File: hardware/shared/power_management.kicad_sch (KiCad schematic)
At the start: 0 parts

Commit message: more kicad work
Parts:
- added C1, C11, C2: 1uF, Capacitor_SMD:C_0402_1005Metric, symbol Device:C
- added C10, C12, C13, C14, C4, C5, C7, C8, C9: 10uF, Capacitor_SMD:C_0603_1608Metric, symbol Device:C
- added C3: 4.7uF, Capacitor_SMD:C_0603_1608Metric, symbol Device:C
- added C6: 100nF, Capacitor_SMD:C_0402_1005Metric, symbol Device:C
- added D1: RED err, LED_SMD:LED_0603_1608Metric, symbol Device:LED
- added D2: GREEN chg, LED_SMD:LED_0603_1608Metric, symbol Device:LED
- added J3: USB4720-03-A, obc:GCT_USB4720-03-A_REVA, symbol obc:USB4720-03-A
- added J4: BT1 1S Li-Po, Connector_JST:JST_PH_S2B-PH-K_1x02_P2.00mm_Horizontal, symbol Connector_Generic:Conn_01x02
- added L1, L2, L3: 2.2uH, Inductor_SMD:L_Murata_DFE201610P, symbol Device:L
- added R6: 10k 1%, Resistor_SMD:R_0402_1005Metric, symbol Device:R
- added R7: 300k 1%, Resistor_SMD:R_0402_1005Metric, symbol Device:R
- added SW5: PWR, Button_Switch_SMD:SW_SPST_EVQP7C, symbol Switch:SW_Push
- added U2: NPM1300-CAAA-R, obc:BGA35N44X41P5X7_237X307X51, symbol obc:NPM1300-CAAA-R
- added U7: TPS610997, symbol obc:TPS610997
- added U8: USBLC6-2SC6, Package_TO_SOT_SMD:SOT-23-6, symbol Power_Protection:USBLC6-2SC6
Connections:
- new net: SW5.2, U2.D4 (SHPHLD)
- new net: L3.2, U7.5 (SW)
- new net: L1.1, U2.B7 (SW1)
- new net: D1.1 (K), U2.A1 (LED0)
- new net: D2.1 (K), U2.A2 (LED1)
- new net: R6.1, U2.D3 (NTC)
- new net: L2.1, U2.D7 (SW2)
- new net: R7.1, U2.E1 (VSET2)
- new net +1V8_MAG: C10.1, C9.1, U2.A4 (LSOUT1/VOUTLDO1)
- new net +3V3: C6.1, C8.1, L2.2, U2.B4 (LSIN1/VINLDO1), U2.B5 (LSIN2/VINLDO2), U2.C6 (VOUT2), U2.E4 (VDDIO)
- new net +3V3_GPS: C11.1, U2.A5 (LSOUT2/VOUTLDO2)
- new net +3V3_SD: C7.1, L1.2, U2.B6 (VOUT1)
- new net +5V_DISP: C13.1, C14.1, U7.2 (VOUT)
- new net DISP_5V_EN: U7.4 (EN)
- new net GND: C1.2, C10.2, C11.2, C12.2, C13.2, C14.2, C2.2, C3.2, C4.2, C5.2, C6.2, C7.2, C8.2, C9.2, J3.A1_B12 (GND_A), J3.B1_A12 (GND_B), J3.SH1 (SHIELD), J3.SH2 (SHIELD), J3.SH3 (SHIELD), J3.SH4 (SHIELD), J3.SH5 (SHIELD), J3.SH6 (SHIELD), J4.2 (Pin_2), R6.2, R7.2, SW5.1, U2.A6 (AVSS), U2.A7 (PVSS1), U2.E2 (VSET1), U2.E7 (PVSS2), U7.1 (GND), U7.3 (FB), U7.7 (PAD), U8.2 (GND)
- new net PMIC_INT: U2.C4 (GPIO3)
- new net SCL: U2.E3 (SCL)
- new net SDA: U2.E5 (SDA)
- new net USB_CC1: J3.A5 (CC1), U2.D5 (CC1)
- new net USB_CC2: J3.B5 (CC2), U2.B3 (CC2)
- new net USB_DM: J3.A7 (DN1), J3.B7 (DN2), U8.1 (I/O1), U8.6 (I/O1)
- new net USB_DP: J3.A6 (DP1), J3.B6 (DP2), U8.3 (I/O2), U8.4 (I/O2)
- new net VBAT: C3.1, J4.1 (Pin_1), U2.D1 (VBAT), U2.D2 (VBAT)
- new net VBUS: C1.1, J3.A4_B9 (VBUS_A), J3.B4_A9 (VBUS_B), U2.B1 (VBUS), U2.B2 (VBUS), U8.5 (VBUS)
- new net VBUS_MCU: C2.1, U2.C3 (VBUSOUT)
- new net VSYS: C12.1, C4.1, C5.1, D1.2 (A), D2.2 (A), L3.1, U2.C1 (VSYS), U2.C2 (VSYS), U2.C7 (PVDD), U7.6 (VIN)
- no-connect marks 0 -> 6
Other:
- note added: "5V DISPLAY BOOST — TPS610997"
- note added: "BATTERY"
- note added: "ERC FLAGS"
- note added: "PVDD"
- note added: "USB-C"
- note added: "VBUSOUT"
- note added: "VSET2=300k -> BUCK2 3.3V at startup (main rail). VSET1=GND -> BUCK1 OFF at startup; fw sets 3.3V, enables only to mount SD (power gate). LDSW1 = LDO 1.8V from +3V3 -> BMM350 VDD. LDSW2 = load switch +3V3 -> +3V3_GPS. Both OFF at boot - fw enables via I2C (0x6B). Charge current set in fw; NTC fixed 10k (no pack thermistor) -> disable NTC monitor or treat 25C. LED0 = charger error, LED1 = charging 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"
- note added: "nPM1300 — CHARGER + BUCKS + LDSW"
- note added: "pack NTC: n/a (R6 fixed)"
- company: (none) -> OpenBikeComputer
- title: (none) -> Power Management

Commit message: more pcb work - add baseboard remove Proto
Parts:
- removed C1, C11, C2: 1uF, Capacitor_SMD:C_0402_1005Metric, symbol Device:C
- removed C10, C4, C5, C7, C8, C9: 10uF, Capacitor_SMD:C_0603_1608Metric, symbol Device:C
- removed C3: 4.7uF, Capacitor_SMD:C_0603_1608Metric, symbol Device:C
- removed C6: 100nF, Capacitor_SMD:C_0402_1005Metric, symbol Device:C
- removed D1: RED err, LED_SMD:LED_0603_1608Metric, symbol Device:LED
- removed D2: GREEN chg, LED_SMD:LED_0603_1608Metric, symbol Device:LED
- removed J3: USB4720-03-A, obc:GCT_USB4720-03-A_REVA, symbol obc:USB4720-03-A
- removed L1, L2: 2.2uH, Inductor_SMD:L_Murata_DFE201610P, symbol Device:L
- removed R6: 10k 1%, Resistor_SMD:R_0402_1005Metric, symbol Device:R
- removed R7: 300k 1%, Resistor_SMD:R_0402_1005Metric, symbol Device:R
- removed SW5: PWR, Button_Switch_SMD:SW_SPST_EVQP7C, symbol Switch:SW_Push
- removed U8: USBLC6-2SC6, Package_TO_SOT_SMD:SOT-23-6, symbol Power_Protection:USBLC6-2SC6
- added J3: Conn_01x06, symbol Connector_Generic:Conn_01x06
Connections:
- net GND: now also U2.D3 (NTC), J3.2 (Pin_2); no longer U2.A6 (AVSS), U2.A7 (PVSS1), U2.E2 (VSET1), U2.E7 (PVSS2)
- net SCL: now also U2.E5 (SDA); no longer U2.E3 (SCL)
- net SDA: now also U2.E3 (SCL); no longer U2.E5 (SDA)
- net USB_CC1: now also J3.3 (Pin_3)
- net USB_CC2: now also J3.4 (Pin_4)
- net USB_DM: now also J3.6 (Pin_6)
- net USB_DP: now also J3.5 (Pin_5)
- net VBUS: now also J3.1 (Pin_1)
- net VSYS: no longer U2.C1 (VSYS), U2.C2 (VSYS), U2.C7 (PVDD)
- net +1V8_MAG: no longer names the net of U2.A4 (LSOUT1/VOUTLDO1)
- removed net +3V3: U2.B4 (LSIN1/VINLDO1), U2.B5 (LSIN2/VINLDO2), U2.C6 (VOUT2), U2.E4 (VDDIO)
- net +3V3_GPS: no longer names the net of U2.A5 (LSOUT2/VOUTLDO2)
- net +3V3_SD: no longer names the net of U2.B6 (VOUT1)
- net PMIC_INT: no longer names the net of U2.C4 (GPIO3)
- net VBUS_MCU: no longer names the net of U2.C3 (VBUSOUT)
- no-connect marks 6 -> 3
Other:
- note added: "BUCK1 for SD Card"
- note added: "BUCK2 for everything else, 3.2V to make display very happy"
- note added: "LDO1 for 1.8V Compass"
- note added: "Loadswitch 2 for GPS"
- note removed: "PVDD"
- note removed: "VBUSOUT"
- note removed: "VSET2=300k -> BUCK2 3.3V at startup (main rail). VSET1=GND -> BUCK1 OFF at startup; fw sets 3.3V, enables only to mount SD (power gate). LDSW1 = LDO 1.8V from +3V3 -> BMM350 VDD. LDSW2 = load switch +3V3 -> +3V3_GPS. Both OFF at boot - fw enables via I2C (0x6B). Charge current set in fw; NTC fixed 10k (no pack thermistor) -> disable NTC monitor or treat 25C. LED0 = charger error, LED1 = charging 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"
- note removed: "pack NTC: n/a (R6 fixed)"
- moved on the sheet: C12, C13, C14, J4, L3, U7

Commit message: more schematic progress and some library additions
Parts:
- removed C12, C13, C14: 10uF, Capacitor_SMD:C_0603_1608Metric, symbol Device:C
- removed L3: 2.2uH, Inductor_SMD:L_Murata_DFE201610P, symbol Device:L
- added C1, C10, C2, C3, C4, C5, C8, C9: 10u, symbol Device:C_Small
- added C6: 1u, symbol Device:C_Small
- added C7: 100n, symbol Device:C_Small
- added L1, L2, L5: 2.2uH, symbol Device:L_Small
- added NT1, NT2: NetTie_2, symbol Device:NetTie_2
- added R1: 0R, symbol Device:R_Small
- added R2: 150k, symbol Device:R_Small
- U7: footprint (none) -> Package_SON:WSON-6-1EP_2x2mm_P0.65mm_EP1x1.6mm; MPN (none) -> TPS610997DRVR; Manufacturer (none) -> Texas Instruments
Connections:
- net +5V_DISP: now also U7.B2 (VOUT), C10.1, C9.1; no longer U7.2 (VOUT)
- net DISP_5V_EN: now also U7.C1 (EN); no longer U7.4 (EN)
- net GND: now also U2.A6 (AVSS), U7.A2 (GND), U7.C2 (FB), C10.2, C5.2, C6.2, C7.2, C8.2, C9.2, NT1.2, NT2.2, R1.2, R2.2; no longer U7.1 (GND), U7.3 (FB), U7.7 (PAD)
- net VBAT: now also U7.A1 (VIN), C8.1, L5.1
- net +1V8_MAG: now reaches U2.A4 (LSOUT1/VOUTLDO1)
- net +3V2_GPS: now reaches U2.A5 (LSOUT2/VOUTLDO2)
- net PVSS1: now reaches U2.A7 (PVSS1)
- net PVSS1: now also C1.2, C3.2, NT1.1
- net +3V2: now reaches U2.B4 (LSIN1/VINLDO1)
- net +3V2: now also U2.B5 (LSIN2/VINLDO2), U2.C6 (VOUT2), U2.E4 (VDDIO), C2.1, C7.1, L2.1
- net +3V3_SD: now reaches U2.B6 (VOUT1)
- net +3V3_SD: now also C1.1, L1.1
- net at U2.B7 (SW1): now also L1.2
- net at U2.C1 (VSYS): now also U2.C2 (VSYS), U2.C7 (PVDD), C3.1, C4.1, C5.1
- net at U2.C3 (VBUSOUT): now also C6.1
- net at U2.D7 (SW2): now also L2.2
- net at U2.E1 (VSET2): now also R2.1
- net at U2.E2 (VSET1): now also R1.1
- net PVSS2: now reaches U2.E7 (PVSS2)
- net PVSS2: now also C2.2, C4.2, NT2.1
- removed net VSYS: U7.6 (VIN)
- new net: L5.2, U7.B1 (SW)
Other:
- note added: "BUCK2 for everything else, 3.2V to make display happy"
- note removed: "BUCK2 for everything else, 3.2V to make display very happy"
- moved on the sheet: U2

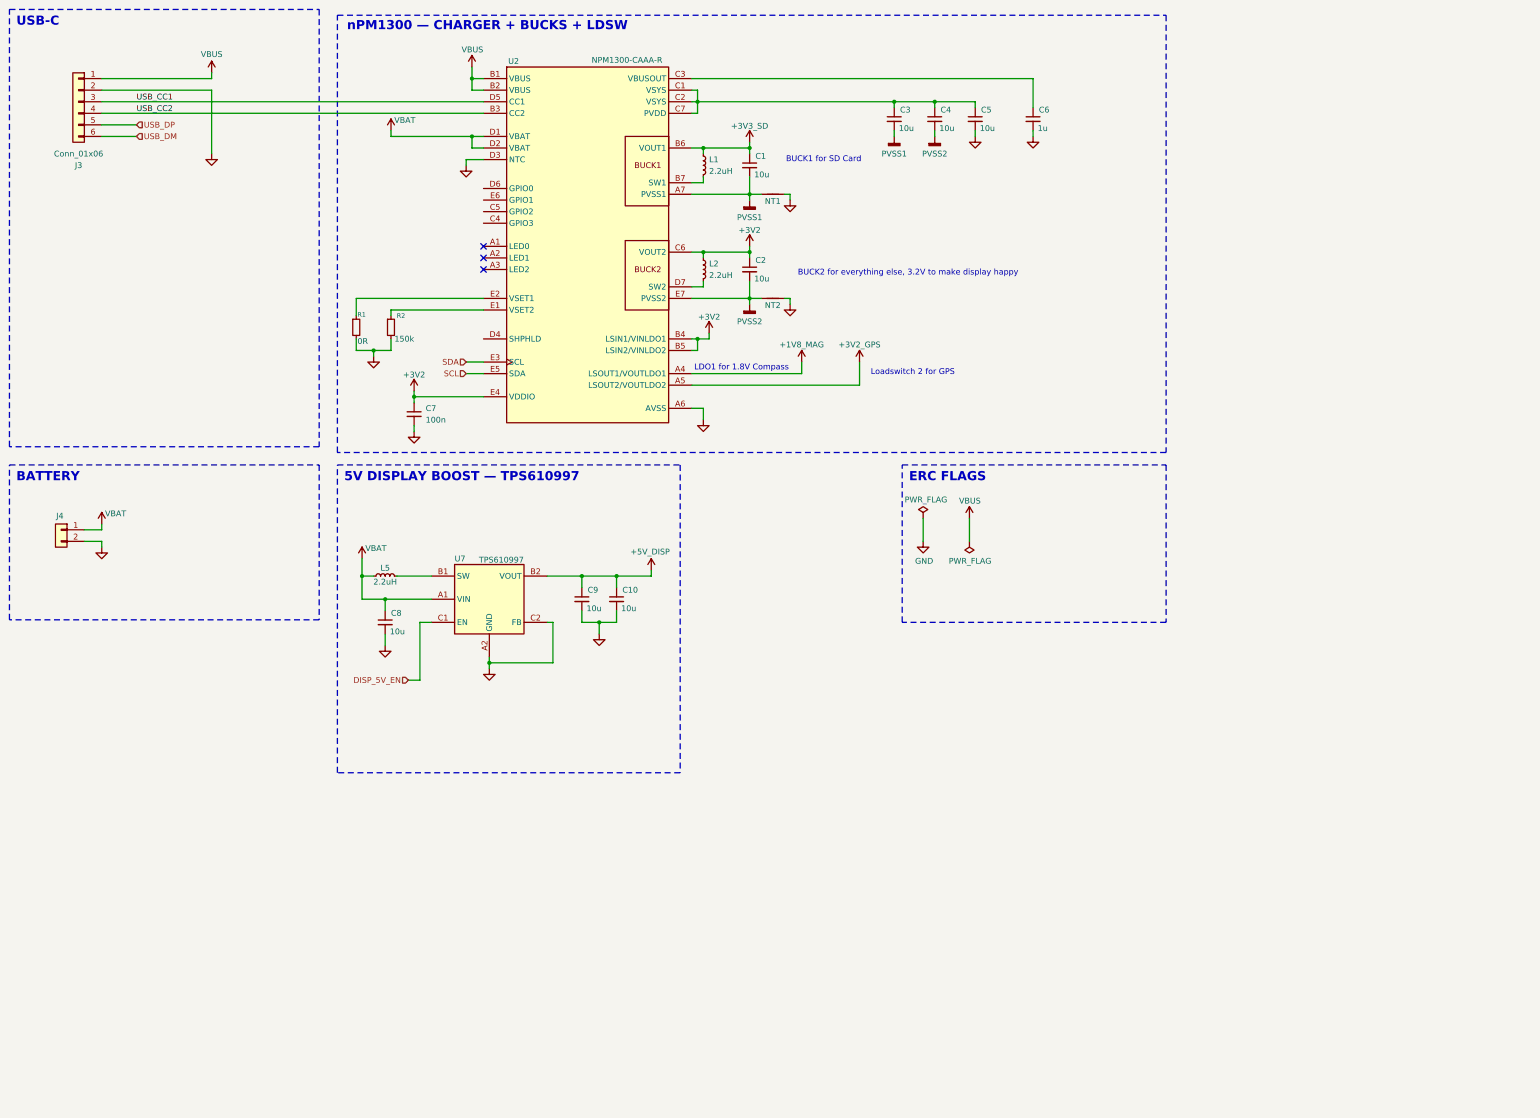
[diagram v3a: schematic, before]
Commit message: hardware: complete modular main-board and USB schematics
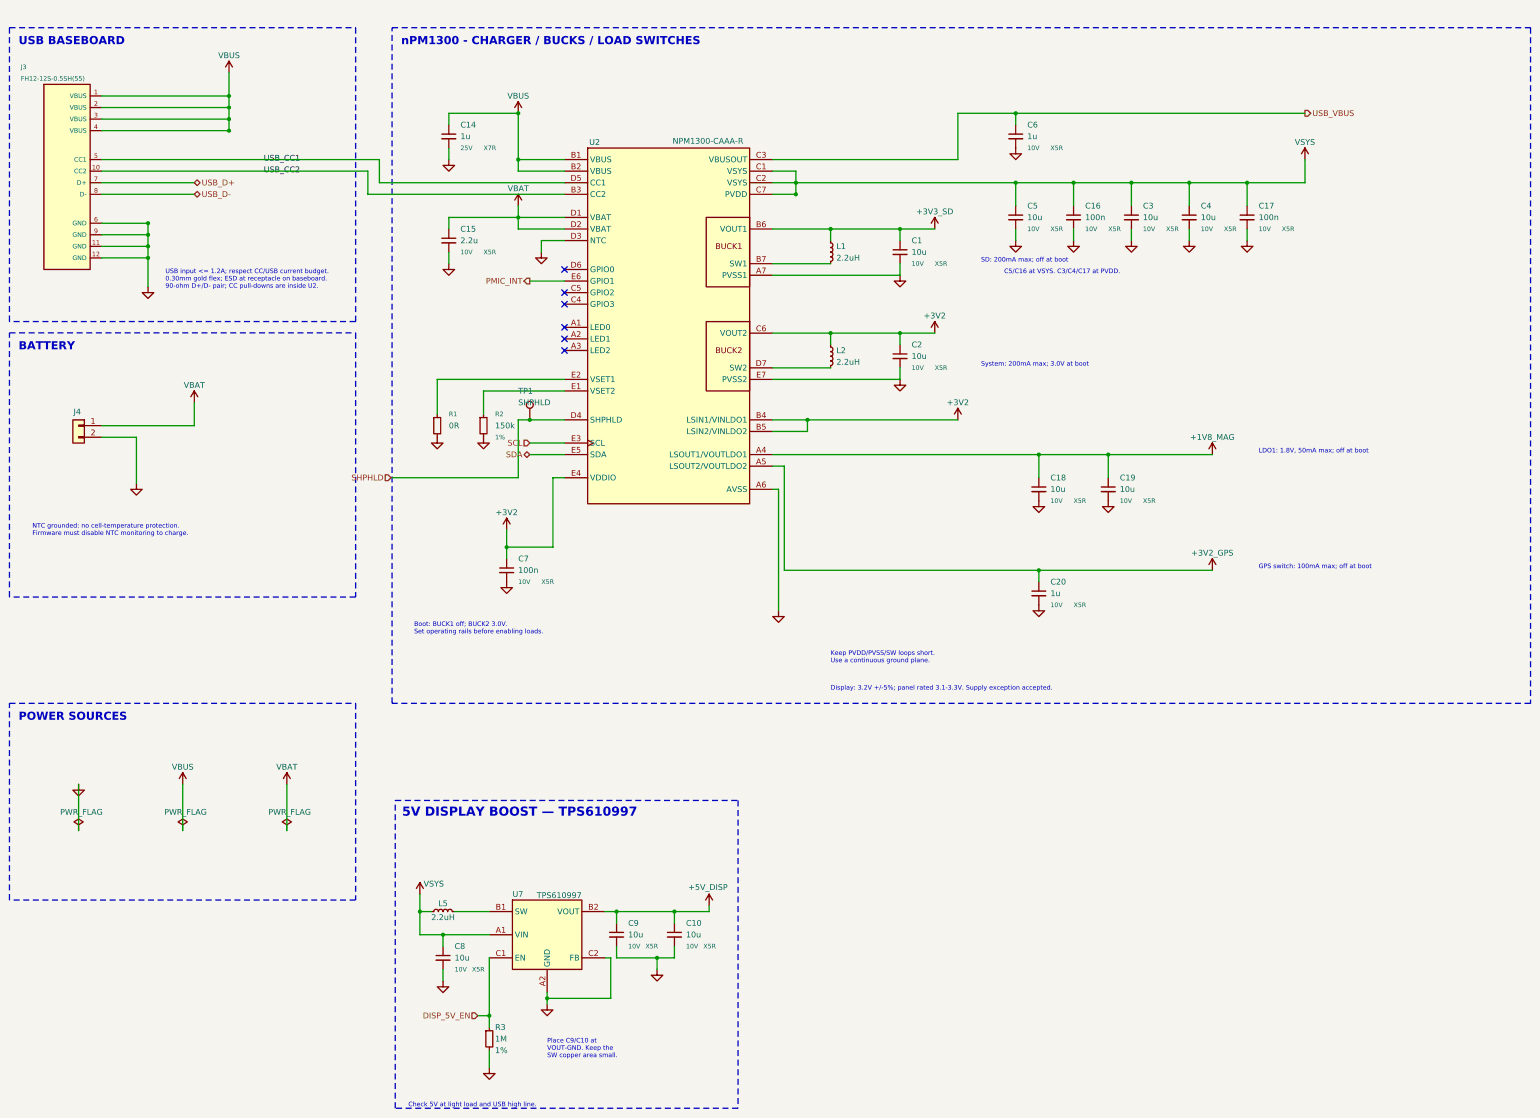
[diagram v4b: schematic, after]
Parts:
- removed NT1, NT2: NetTie_2, symbol Device:NetTie_2
- added C14, C20: 1u, Capacitor_SMD:C_0603_1608Metric, symbol Device:C_Small
- added C15: 2.2u, Capacitor_SMD:C_0603_1608Metric, symbol Device:C_Small
- added C16, C17: 100n, Capacitor_SMD:C_0402_1005Metric, symbol Device:C_Small
- added C18, C19: 10u, Capacitor_SMD:C_0805_2012Metric, symbol Device:C_Small
- added R3: 1M, Resistor_SMD:R_0402_1005Metric, symbol Device:R_Small
- added TP1: SHPHLD, TestPoint:TestPoint_Pad_D1.0mm, symbol Connector:TestPoint
- C1, C2: footprint (none) -> Capacitor_SMD:C_0805_2012Metric; Capacitance at bias (none) -> 4uF to 20uF effective; ESR <=50mOhm; Dielectric (none) -> X5R; Tolerance (none) -> 10%; Voltage (none) -> 10V
- C10, C9: footprint (none) -> Capacitor_SMD:C_0805_2012Metric; Capacitance at bias (none) -> Minimum 5uF at 5.2V over tolerance and temperature; Dielectric (none) -> X5R; Tolerance (none) -> 10%; Voltage (none) -> 10V
- C3, C4, C5: footprint (none) -> Capacitor_SMD:C_0805_2012Metric; Capacitance at bias (none) -> Minimum 4uF at 5.5V; Dielectric (none) -> X5R; Tolerance (none) -> 10%; Voltage (none) -> 10V
- C6: footprint (none) -> Capacitor_SMD:C_0603_1608Metric; Dielectric (none) -> X5R; Tolerance (none) -> 10%; Voltage (none) -> 10V
- C7: footprint (none) -> Capacitor_SMD:C_0402_1005Metric; Dielectric (none) -> X5R; Tolerance (none) -> 10%; Voltage (none) -> 10V
- C8: footprint (none) -> Capacitor_SMD:C_0805_2012Metric; Capacitance at bias (none) -> Minimum 1uF at 5.5V over tolerance and temperature; Dielectric (none) -> X5R; Tolerance (none) -> 10%; Voltage (none) -> 10V
- J3: value Conn_01x06 -> FH12-12S-0.5SH(55); footprint (none) -> Connector_FFC-FPC:Hirose_FH12-12S-0.5SH_1x12-1MP_P0.50mm_Horizontal; symbol Connector_Generic:Conn_01x06 -> obc:USB_FLEX_12; Contact Side (none) -> Bottom; Current Rating (none) -> 0.5A/contact; use 70% rating for populated power contact ba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; FPC Thickness (none) -> 0.30 +/-0.05mm; MPN (none) -> FH12-12S-0.5SH(55); Manufacturer (none) -> Hirose; USB Input Limit (none) -> 1.2A max setting (1.32A with PMIC tolerance)
- J4: value BT1 1S Li-Po -> 1S Li-Po; footprint Connector_JST:JST_PH_S2B-PH-K_1x02_P2.00mm_Horizontal -> obc:JST_ACH_2pin; MPN S2B-PH-K-S -> BM02B-ACHSS-GAN-ETF; Mating contact (none) -> SACH-003G-P0.2; Mating housing (none) -> ACHR-02V-S; Pinout (none) -> 1=VBAT; 2=GND; confirm battery harness polarity; Wire (none) -> AWG28 for 2A rating
- L1, L2, L5: footprint (none) -> obc:Wurth_74404024022_2.5x2.0mm; DCR (none) -> 80mOhm +/-20%; MPN (none) -> 74404024022; Manufacturer (none) -> Wurth Elektronik; Rated Current (none) -> 1.65A (40K rise); Saturation Current (none) -> 1.9A typ (30% L drop); Tolerance (none) -> 20%
- R1: footprint (none) -> Resistor_SMD:R_0402_1005Metric; Power (none) -> 63mW; Technology (none) -> Thick film; Tolerance (none) -> Jumper; Voltage (none) -> 50V
- R2: footprint (none) -> Resistor_SMD:R_0402_1005Metric; Power (none) -> 63mW; Technology (none) -> Thick film; Tolerance (none) -> 1%; Voltage (none) -> 50V
- U7: footprint Package_SON:WSON-6-1EP_2x2mm_P0.65mm_EP1x1.6mm -> obc:TI_YFF0006_0.884x1.226mm_P0.4mm; MPN TPS610997DRVR -> TPS610997YFFR
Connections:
- net PVSS1 is gone; now on net GND: C1.2, C3.2, U2.A7 (PVSS1)
- net PVSS2 is gone; now on net GND: C2.2, C4.2, U2.E7 (PVSS2)
- net USB_DM is gone; now on net GND: J3.6 (GND)
- net USB_DP is gone; now on net USB_CC1: J3.5 (CC1)
- net +1V8_MAG: now also C18.1, C19.1
- net +3V2_GPS: now also C20.1
- net DISP_5V_EN: now also R3.1
- net GND: now also J3.11 (GND), J3.12 (GND), J3.9 (GND), C14.2, C15.2, C16.2, C17.2, C18.2, C19.2, C20.2, R3.2; no longer J3.2 (Pin_2)
- net SCL: now also U2.E3 (SCL); no longer U2.E5 (SDA)
- net SDA: now also U2.E5 (SDA); no longer U2.E3 (SCL)
- net USB_CC1: no longer J3.3 (Pin_3)
- net USB_CC2: now also J3.10 (CC2); no longer J3.4 (Pin_4)
- net VBAT: now also C15.1; no longer C8.1, L5.1, U7.A1 (VIN)
- net VBUS: now also J3.2 (VBUS), J3.3 (VBUS), J3.4 (VBUS), C14.1
- net VSYS: now reaches C3.1, C4.1, C5.1, U2.C1 (VSYS), U2.C2 (VSYS), U2.C7 (PVDD)
- net VSYS: now also C8.1, L5.1, U7.A1 (VIN), C16.1, C17.1
- net USB_VBUS: now reaches C6.1, U2.C3 (VBUSOUT)
- net SHPHLD: now reaches U2.D4 (SHPHLD)
- net SHPHLD: now also TP1.1
- net PMIC_INT: now reaches U2.E6 (GPIO1)
- new net USB_D+: J3.7 (D+)
- new net USB_D-: J3.8 (D-)
- no-connect marks 3 -> 6
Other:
- note added: "Boot: BUCK1 off; BUCK2 3.0V. Set operating rails before enabling loads."
- note added: "C5/C16 at VSYS. C3/C4/C17 at PVDD."
- note added: "Check 5V at light load and USB high line."
- note added: "Display: 3.2V +/-5%; panel rated 3.1-3.3V. Supply exception accepted."
- note added: "GPS switch: 100mA max; off at boot"
- note added: "Keep PVDD/PVSS/SW loops short. Use a continuous ground plane."
- note added: "LDO1: 1.8V, 50mA max; off at boot"
- note added: "NTC grounded: no cell-temperature protection. Firmware must disable NTC monitoring to charge."
- note added: "POWER SOURCES"
- note added: "Place C9/C10 at VOUT-GND. Keep the SW copper area small."
- note added: "SD: 200mA max; off at boot"
- note added: "System: 200mA max; 3.0V at boot"
- note added: "USB BASEBOARD"
- note added: "USB input <= 1.2A; respect CC/USB current budget. 0.30mm gold flex; ESD at receptacle on baseboard. 90-ohm D+/D- pair; CC pull-downs are inside U2."
- note added: "nPM1300 - CHARGER / BUCKS / LOAD SWITCHES"
- note removed: "BUCK1 for SD Card"
- note removed: "BUCK2 for everything else, 3.2V to make display happy"
- note removed: "ERC FLAGS"
- note removed: "LDO1 for 1.8V Compass"
- note removed: "Loadswitch 2 for GPS"
- note removed: "USB-C"
- note removed: "nPM1300 — CHARGER + BUCKS + LDSW"
- moved on the sheet: C1, C10, C2, C3, C4, C5, C6, C7, C8, C9, J4, L1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
